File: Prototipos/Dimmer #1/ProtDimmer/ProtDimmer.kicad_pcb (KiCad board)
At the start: 2 copper layers, 73.7 x 50.8 mm, 22 parts, among them J1 Conn_01x02, J2 Conn_01x02, J3 Conn_01x05, K1 SRD-05VDC-SL-C, Q1 BC548B, Q2 BT137, U1 MOC3021M, U2 EL817

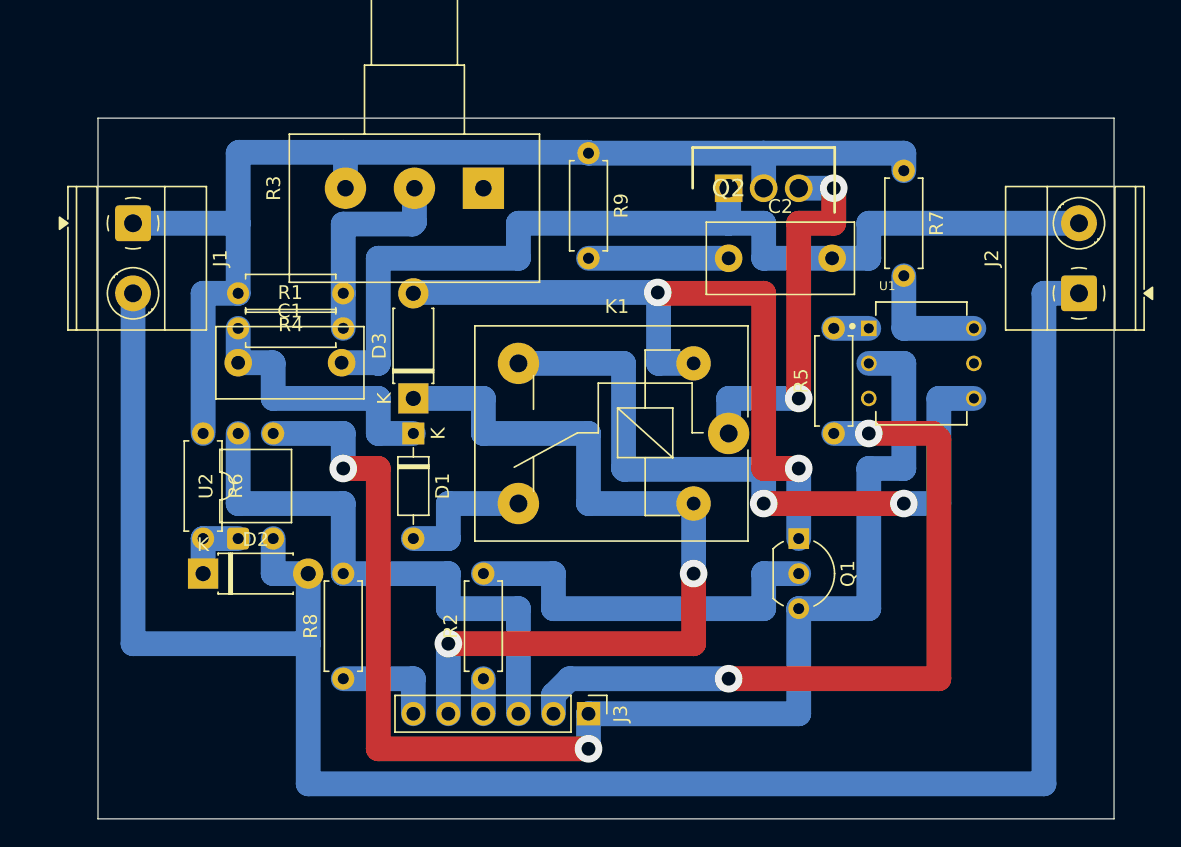
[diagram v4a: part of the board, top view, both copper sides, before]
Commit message: Arreglar texto pcb y agregar letras y números guía
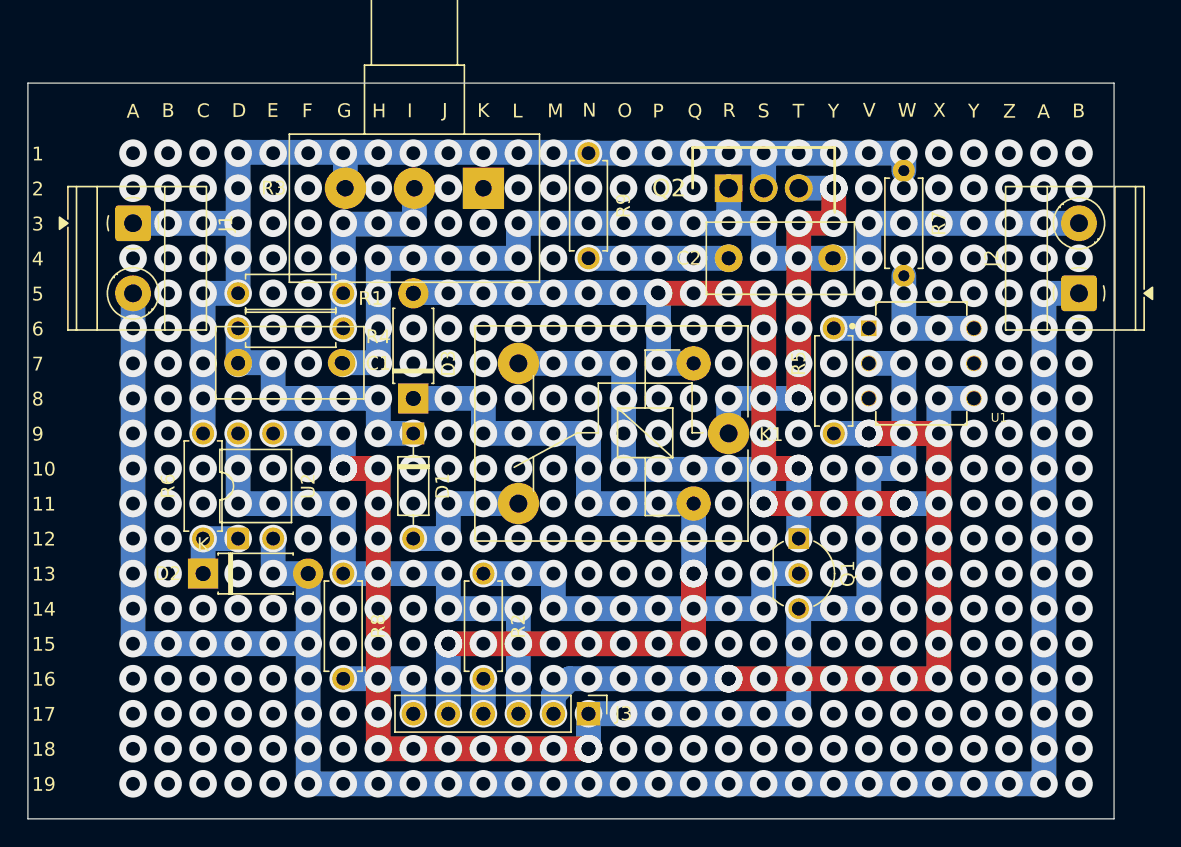
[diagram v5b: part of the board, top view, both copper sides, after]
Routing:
- net unconnected-(U1-NC-Pad5): vias 0 -> 2
- net unconnected-(U1-NC-Pad3): vias 0 -> 2
- net UC_RELAY: vias 0 -> 4
- net Retro_micro: vias 0 -> 9
- net PWM_micro: vias 0 -> 2
- net PWM_MOSFET: vias 0 -> 2
- net PWM_BJT: vias 0 -> 2
- net Net-(R7-Pad2): vias 0 -> 12
- net Net-(R5-Pad2): vias 0 -> 2
- net Net-(R10-Pad1): vias 0 -> 1
- net Net-(R1-Pad2): vias 0 -> 17
- net Net-(Q3-B): vias 0 -> 3
- net Net-(Q1-B): vias 0 -> 5
- net Net-(J3-Pin_1): vias 0 -> 9
- net Net-(D2-K): vias 0 -> 4
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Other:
- board size 73.7 x 50.8 mm -> 78.7 x 53.3 mm
- board text added: "1"
- board text added: "10"
- board text added: "11"
- board text added: "12"
- board text added: "13"
- board text added: "14"
- board text added: "15"
- board text added: "16"
- board text added: "17"
- board text added: "18"
- board text added: "19"
- board text added: "2"
- board text added: "3"
- board text added: "4"
- board text added: "5"
- board text added: "6"
- board text added: "7"
- board text added: "8"
- board text added: "9"
- board text added: "A"
- board text added: "B"
- board text added: "C"
- board text added: "D"
- board text added: "E"
- board text added: "F"
- board text added: "G"
- board text added: "H"
- board text added: "I"
- board text added: "J"
- board text added: "K"
- board text added: "L"
- board text added: "M"
- board text added: "N"
- board text added: "O"
- board text added: "P"
- board text added: "Q"
- board text added: "R"
- board text added: "S"
- board text added: "T"
- board text added: "V"
- board text added: "W"
- board text added: "X"
- board text added: "Y"
- board text added: "Z"
